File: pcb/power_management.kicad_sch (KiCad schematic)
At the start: 11 parts

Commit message: feat: generate KiCad schematics from atopile netlist
scripts/gen_schematics.py generates all 7 hierarchical KiCad schematic
files (root + 6 sub-sheets) from elec/build/default.net:

- Synthesizes box symbols from netlist libpart pin counts
- Pure label-per-pin connectivity (no wires)
- Hierarchical labels for inter-sheet nets
- Deterministic UUIDs from atopile tstamps
- Built-in oracle verifies connectivity partition isomorphism
- No-connect markers on intentionally-unconnected pins

Oracle: ORACLE PASS — 346 pin assignments, 73 multi-node nets,
connectivity partitions isomorphic.

Integrated into Makefile via 'make schematics' target.
Manifest entry added per repo convention.
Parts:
- removed C_BOOT_BUCK: 10nF 50V, Capacitor_SMD:C_0603_1608Metric, symbol Device:C
- removed C_IN_BUCK: 2.2µF 100V, Capacitor_SMD:C_1210_3225Metric, symbol Device:C
- removed C_IN_LDO: 10µF 25V, Capacitor_SMD:C_0805_2012Metric, symbol Device:C
- removed C_OUT_BUCK1, C_OUT_BUCK2: 22µF 25V, Capacitor_SMD:C_1206_3216Metric, symbol Device:C
- removed C_OUT_LDO: 22µF 10V, Capacitor_SMD:C_0805_2012Metric, symbol Device:C
- removed L_BUCK: 6.8µH, Inductor_SMD:L_Bourns_SRP1038A, symbol Device:L
- removed R_FB1: 100kΩ, Resistor_SMD:R_0603_1608Metric, symbol Device:R
- removed R_FB2: 7.15kΩ, Resistor_SMD:R_0603_1608Metric, symbol Device:R
- removed U_BUCK: LMR51430XDDCR, Package_TO_SOT_SMD:SOT-23-6, symbol LMR51430:LMR51430X
- removed U_LDO: XC6220B331MR-G, Package_TO_SOT_SMD:SOT-25, symbol XC6220:XC6220B331MR-G
- added U15: LMR51430XDDCR, Package_TO_SOT_SMD:SOT-23-6, symbol LMR51430XDDCR
- added U16, U19, U20: GRM32ER71H106KA12L, Capacitor_SMD:C_1210_3225Metric, symbol GRM32ER71H106KA12L
- added U17, U24, U25: GRM188R71E104KA01D, Capacitor_SMD:C_0603_1608Metric, symbol GRM188R71E104KA01D
- added U18: SRP1265A-220M, Inductor_SMD:L_Bourns_SRP1265A, symbol SRP1265A-220M
- added U21, U22: RC0603FR-07140KL, Resistor_SMD:R_0603_1608Metric, symbol RC0603FR-07140KL
- added U23: XC6220B331MR-G, Package_TO_SOT_SMD:SOT-23-5, symbol XC6220B331MR-G
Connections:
- new net +15V: U18.2, U19.1, U20.1, U21.1, U23.2, U23.3, U24.1
- new net +3V3: U23.5, U25.1
- new net boot: U15.6, U17.1
- new net fb: U15.4, U21.2, U22.1
- new net gnd: U15.1, U16.2, U19.2, U20.2, U22.2, U23.1, U24.2, U25.2
- new net power_mgmt-vcc: U15.3, U15.5, U16.1
- new net sw: U15.2, U17.2, U18.1
- no-connect marks 0 -> 1
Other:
- note removed: "BUCK CONVERTER DESIGN NOTES: Vout = 1.0V × (1 + R_FB1/R_FB2) = 1.0V × (1 + 100k/7.15k) = 15.0V fsw = 2.1MHz (fixed) L = 6.8µH (SRP1038A) Cout = 44µF (2×22µF) Cin = 2.2µF 100V Thermal: Rθja = 45°C/W (SOT-23-6) Max Pdiss at 85°C = 0.89W"
- note removed: "LDO DESIGN NOTES: XC6220B331MR-G - Fixed 3.3V output - 700mA max - 6.5µVrms noise - Dropout: 100mV @ 200mA Cin = 10µF (low ESR) Cout = 22µF (low ESR) Pdiss = (Vin - Vout) × Iout = (15V - 3.3V) × 0.3A = 3.5W (needs heatsinking!) Note: Consider 5V intermediate rail to reduce LDO dissipation"
- note removed: "POWER MANAGEMENT Buck Converter (LMR51430): - Input: DC_BUS (up to 36V from aux tap) - Output: +15V @ 1A - Switching: 2.1MHz - Sync buck topology LDO (XC6220): - Input: +15V (could also be 5V) - Output: +3.3V @ 700mA - Low noise: 6.5µV RMS Reference: - LMR51430_THERMAL_ANALYSIS.md - BOM.md Section 2"
- title: Power Management -> Power_Management

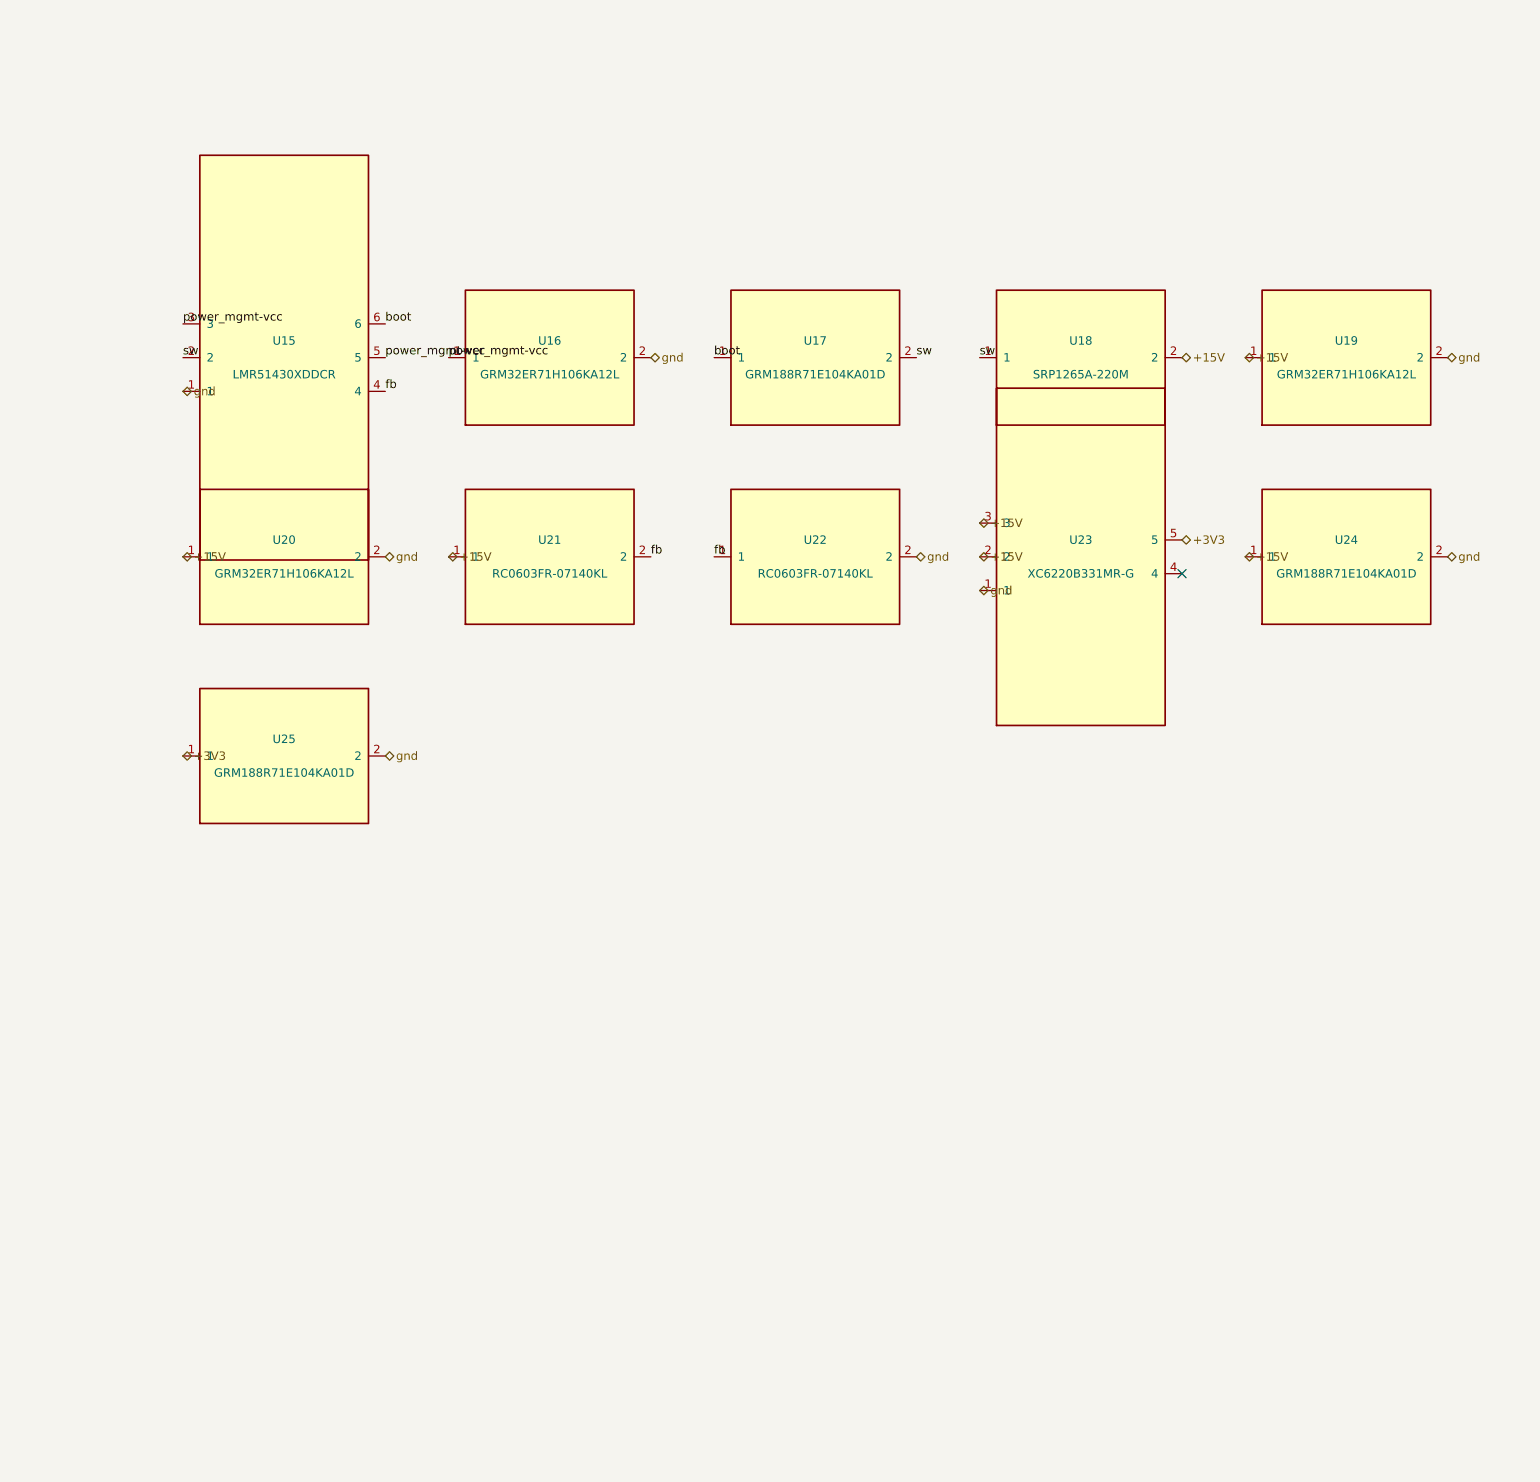
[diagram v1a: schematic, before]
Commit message: chore: regenerate schematics from atopile netlist (#228)
Generated from elec/build/default.net via gen_schematics.py.
Adds 23 new components from discharge (17), aux_supply (4), and
thermal (2) modules that were previously un-mapped and absent.
Root sheet layout re-stacked with dynamic spacing.
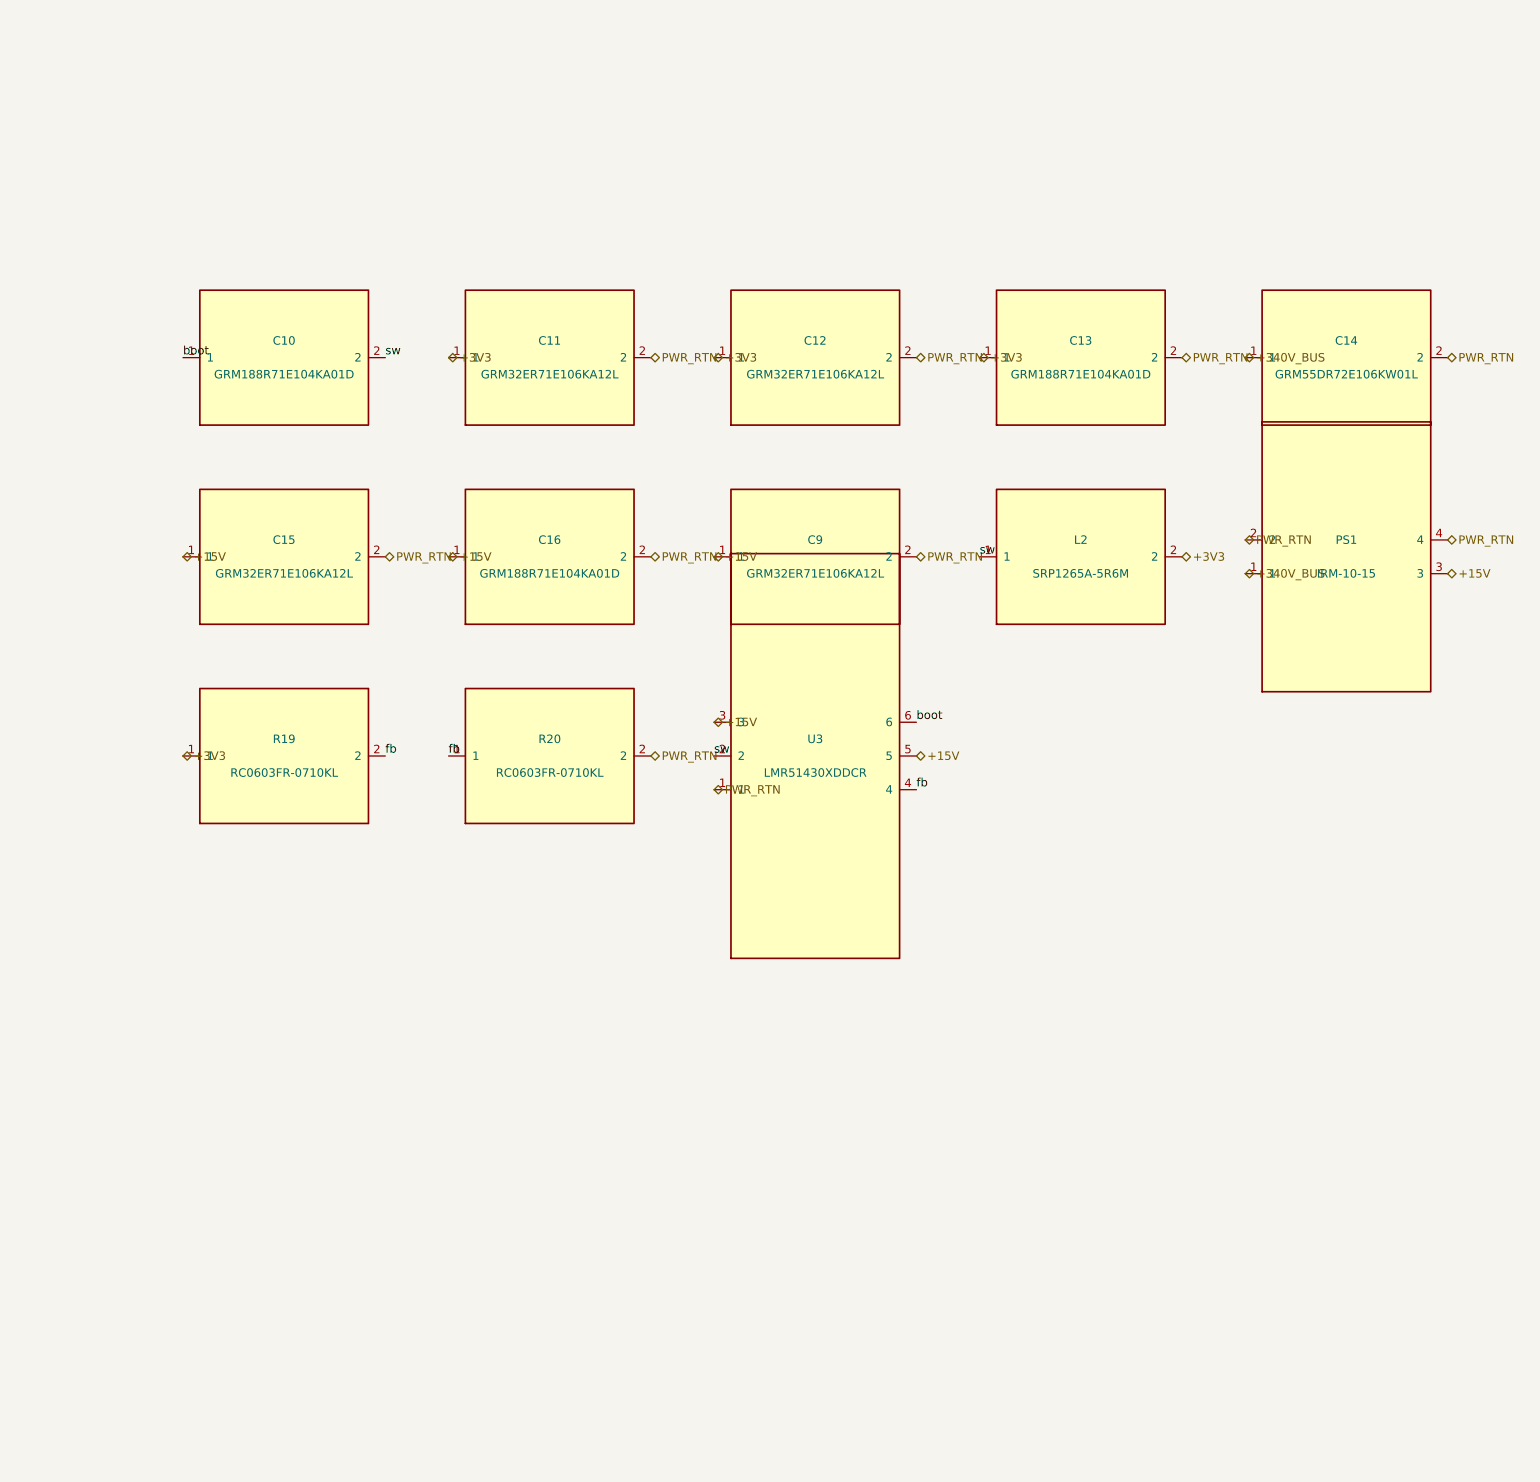
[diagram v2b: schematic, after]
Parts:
- removed U15: LMR51430XDDCR, Package_TO_SOT_SMD:SOT-23-6, symbol LMR51430XDDCR
- removed U16, U19, U20: GRM32ER71H106KA12L, Capacitor_SMD:C_1210_3225Metric, symbol GRM32ER71H106KA12L
- removed U17, U24, U25: GRM188R71E104KA01D, Capacitor_SMD:C_0603_1608Metric, symbol GRM188R71E104KA01D
- removed U18: SRP1265A-220M, Inductor_SMD:L_Bourns_SRP1265A, symbol SRP1265A-220M
- removed U21, U22: RC0603FR-07140KL, Resistor_SMD:R_0603_1608Metric, symbol RC0603FR-07140KL
- removed U23: XC6220B331MR-G, Package_TO_SOT_SMD:SOT-23-5, symbol XC6220B331MR-G
- added C10, C13, C16: GRM188R71E104KA01D, Capacitor_SMD:C_0603_1608Metric, symbol GRM188R71E104KA01D
- added C11, C12, C15, C9: GRM32ER71E106KA12L, Capacitor_SMD:C_1210_3225Metric, symbol GRM32ER71E106KA12L
- added C14: GRM55DR72E106KW01L, Capacitor_SMD:C_2220_5750Metric, symbol GRM55DR72E106KW01L
- added L2: SRP1265A-5R6M, Inductor_SMD:L_Bourns_SRP1265A, symbol SRP1265A-5R6M
- added PS1: IRM-10-15, Converter_ACDC:Converter_ACDC_MeanWell_IRM-10-xx_THT, symbol IRM-10-15
- added R19, R20: RC0603FR-0710KL, Resistor_SMD:R_0603_1608Metric, symbol RC0603FR-0710KL
- added U3: LMR51430XDDCR, Package_TO_SOT_SMD:SOT-23-6, symbol LMR51430XDDCR
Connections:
- net +15V: now also C15.1, C16.1, C9.1, PS1.3, U3.3, U3.5
- net +3V3: now also C11.1, C12.1, C13.1, L2.2, R19.1
- net boot: now also C10.1, U3.6
- net fb: now also R19.2, R20.1, U3.4
- net sw: now also C10.2, L2.1, U3.2
- new net +340V_BUS: C14.1, PS1.1
- new net PWR_RTN: C11.2, C12.2, C13.2, C14.2, C15.2, C16.2, C9.2, PS1.2, PS1.4, R20.2, U3.1
- no-connect marks 1 -> 0
